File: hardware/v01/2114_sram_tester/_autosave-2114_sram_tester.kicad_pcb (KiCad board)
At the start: 2 copper layers, 67.3 x 62.2 mm, 7 parts, among them J1 Conn_02x09_Counter_Clockwise

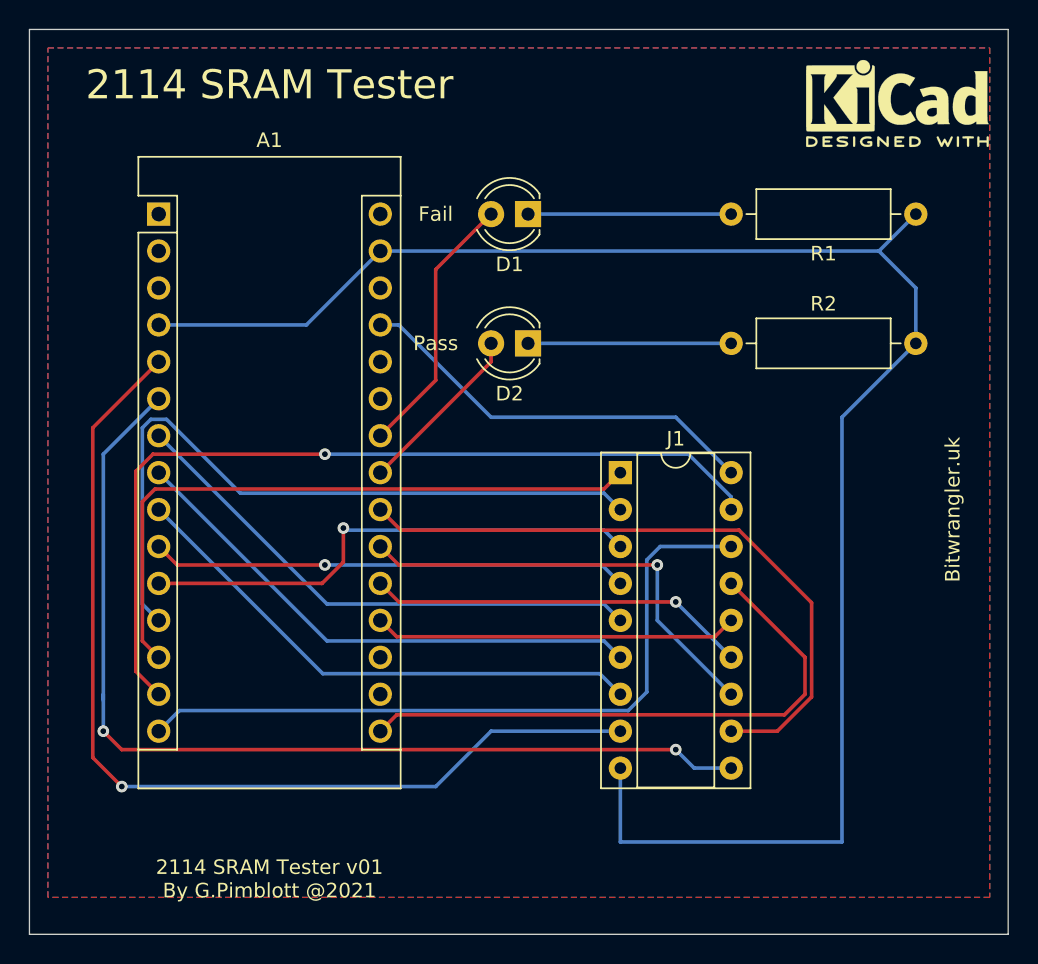
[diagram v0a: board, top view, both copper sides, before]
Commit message: Added button code
Button added to stop/start tests
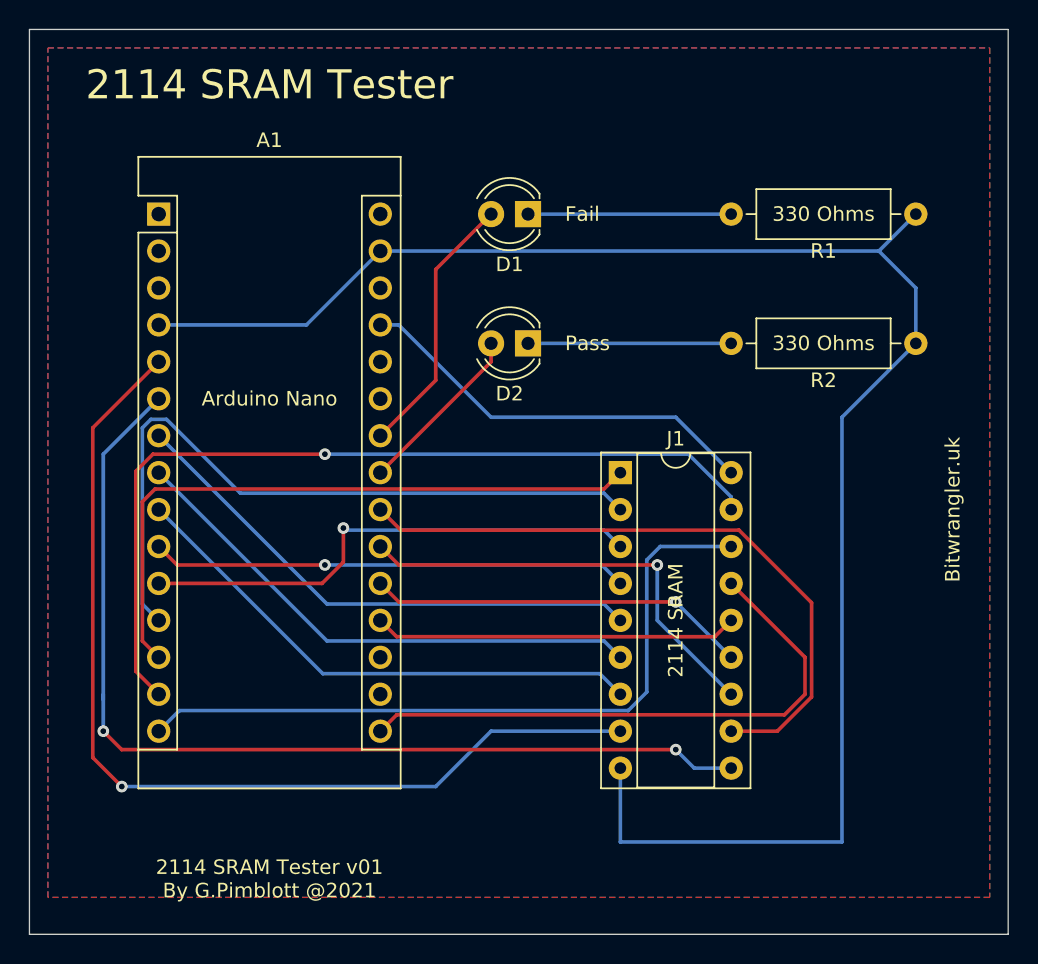
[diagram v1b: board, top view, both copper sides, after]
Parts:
- removed REF**: KiCad-Logo2_5mm_SilkScreen, Symbol:KiCad-Logo2_5mm_SilkScreen
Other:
- board text added: "2114 SRAM"
- board text added: "330 Ohms"
- board text added: "Arduino Nano"
